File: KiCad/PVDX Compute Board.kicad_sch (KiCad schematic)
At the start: 0 parts

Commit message: update draft to 11/13 version
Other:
- added sheet Photodiodes (Photodiodes.kicad_sch)
- note removed: "TODO: 1. DETERMINE PHOTODIODE RESISTANCE 2. SIMPLIFY POWER SWITCHING (REQUIRES DETERMINING 5V AND 1V8 INPUTS?) 3. ADD SBAND"
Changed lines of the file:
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@@
-		)
-	)
-	(text "TODO:\n1. DETERMINE PHOTODIODE RESISTANCE\n2. SIMPLIFY POWER SWITCHING (REQUIRES DETERMINING 5V AND 1V8 INPUTS?)\n3. ADD SBAND"
-		(exclude_from_sim no)
-		(at 69.85 77.978 0)
-		(effects
-			(font
-				(size 3.048 3.048)
-			)
-			(justify left)
 		)
 	)
@@
 				)
 			)
+		)
+	)
+	(sheet
+		(at 127 34.29)
+		(size 30.48 13.97)
+		(exclude_from_sim no)
+		(in_bom yes)
+		(on_board yes)
+		(dnp no)
+		(fields_autoplaced yes)
+		(stroke
+			(width 0.1524)
+			(type solid)
+		)
+		(fill
+			(color 0 0 0 0.0000)
+		)
+		(property "Sheetname" "Photodiodes"
+			(at 127 33.5784 0)
+			(effects
+				(font
+					(size 1.27 1.27)
+				)
+				(justify left bottom)
+			)
+		)
+		(property "Sheetfile" "Photodiodes.kicad_sch"
+			(at 127 48.8446 0)
+			(effects
+				(font
+					(size 1.27 1.27)
+				)
+				(justify left top)
+			)
+		)
+		(instances
+			(project "PVDX Compute Board"
+				(path "/cc5055d2-349f-4e91-a151-9a2f788b119f"
+					(page "4")
+				)
+			)

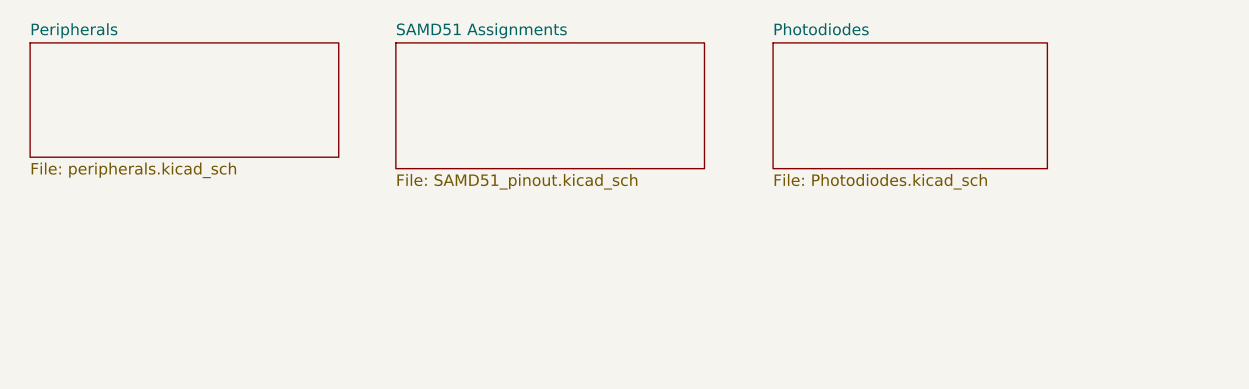
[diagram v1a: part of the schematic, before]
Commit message: updated pins to match new spec and exposed all pins
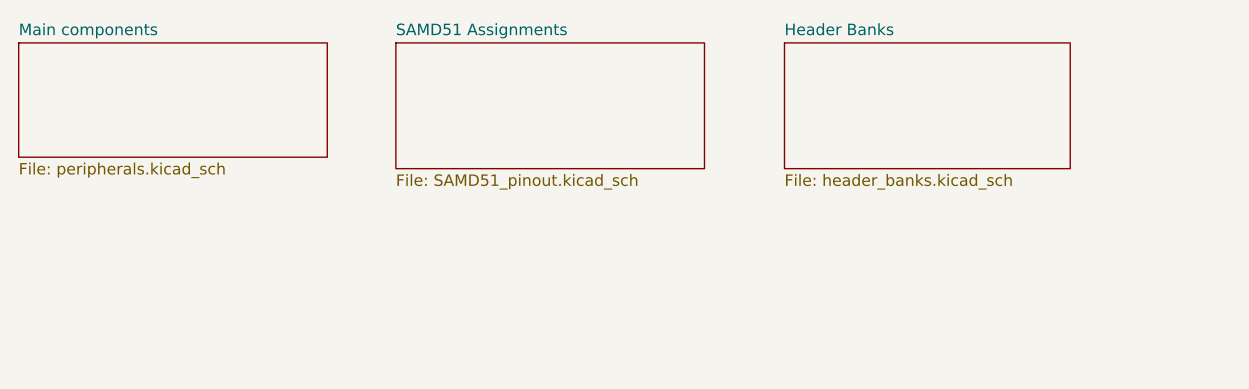
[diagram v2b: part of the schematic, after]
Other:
- sheet Peripherals renamed Main components
- removed sheet Photodiodes
- added sheet Header Banks (header_banks.kicad_sch)
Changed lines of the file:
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@@
 	)
 	(sheet
-		(at 44.45 34.29)
+		(at 43.18 34.29)
 		(size 34.29 12.7)
 		(exclude_from_sim no)
@@
 			(color 0 0 0 0.0000)
 		)
-		(property "Sheetname" "Peripherals"
-			(at 44.45 33.5784 0)
+		(property "Sheetname" "Main components"
+			(at 43.18 33.5784 0)
 			(effects
 				(font
@@
 		)
 		(property "Sheetfile" "peripherals.kicad_sch"
-			(at 44.45 47.5746 0)
+			(at 43.18 47.5746 0)
 			(effects
 				(font
@@
 	)
 	(sheet
-		(at 127 34.29)
-		(size 30.48 13.97)
+		(at 128.27 34.29)
+		(size 31.75 13.97)
 		(exclude_from_sim no)
 		(in_bom yes)
@@
 			(color 0 0 0 0.0000)
 		)
-		(property "Sheetname" "Photodiodes"
-			(at 127 33.5784 0)
+		(property "Sheetname" "Header Banks"
+			(at 128.27 33.5784 0)
 			(effects
 				(font
@@
 			)
 		)
-		(property "Sheetfile" "Photodiodes.kicad_sch"
-			(at 127 48.8446 0)
+		(property "Sheetfile" "header_banks.kicad_sch"
+			(at 128.27 48.8446 0)
 			(effects
 				(font
